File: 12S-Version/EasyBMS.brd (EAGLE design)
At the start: 49 x 100 mm, 156 parts, among them IC1 LM2596S-5.0_NOPB, IC2 LTC6811IG-1#PBF, Q10 BSS84LT1G, Q11 BSS84LT1G, Q12 BSS84LT1G, Q13 BSS84LT1G, Q2 BSS84LT1G, Q3 BSS84LT1G, Q4 BSS84LT1G, Q5 BSS84LT1G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

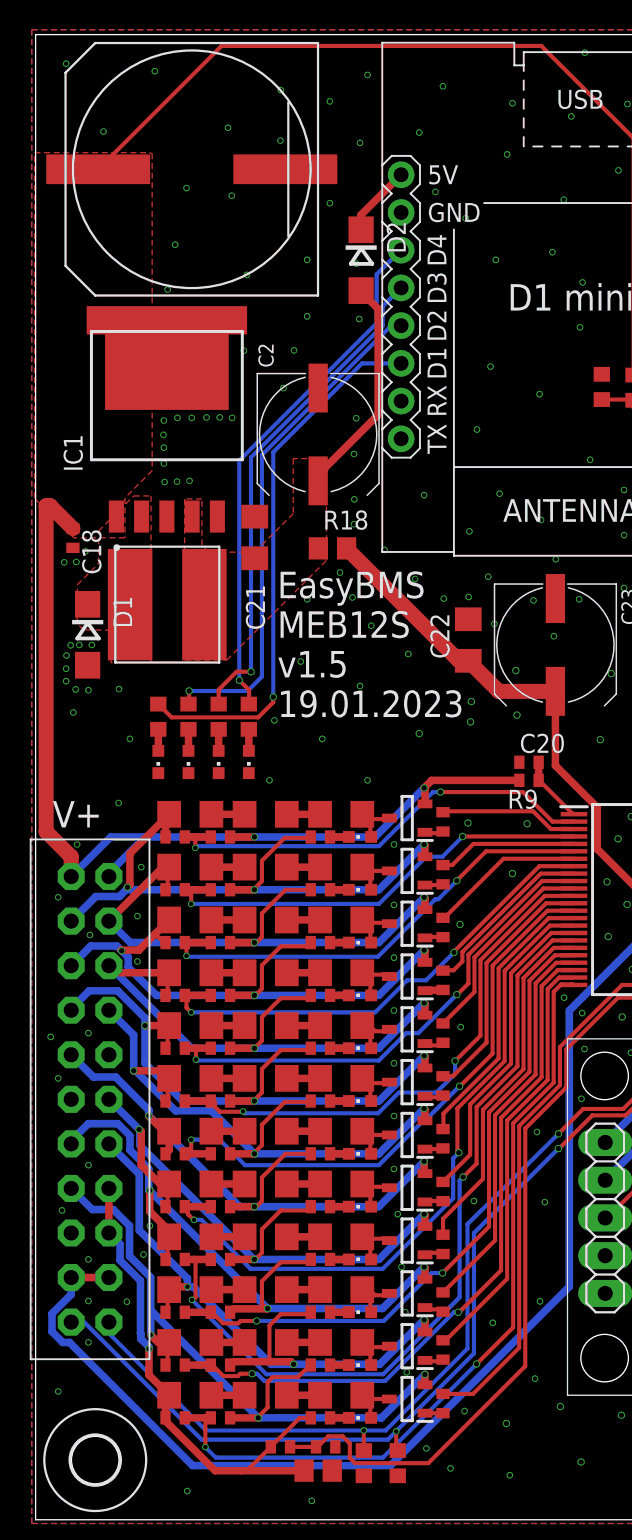
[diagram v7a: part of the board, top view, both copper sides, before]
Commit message: moved some parts a bit to solve collisions
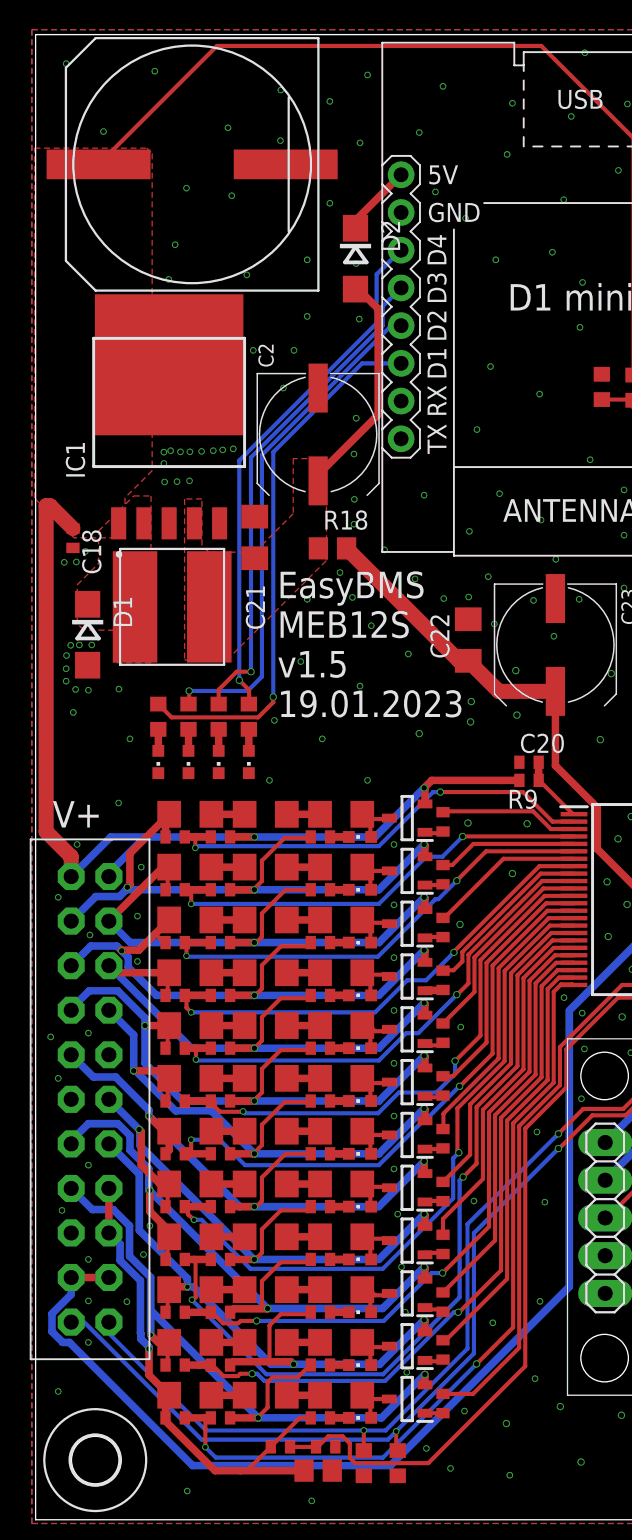
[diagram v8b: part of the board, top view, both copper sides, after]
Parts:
- moved IC1 0.48 mm to (8.99, 73.2)
- moved D2 0.39 mm to (21.5, 84.9)
- moved L1 0.36 mm to (9.19, 61.5)
- moved C24 0.33 mm to (10.5, 91.3)
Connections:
- net GND: no longer IC1.7, IC1.8
